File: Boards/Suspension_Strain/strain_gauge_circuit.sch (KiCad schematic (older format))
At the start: 9 parts, among them U101 MCP6001T-I-LT

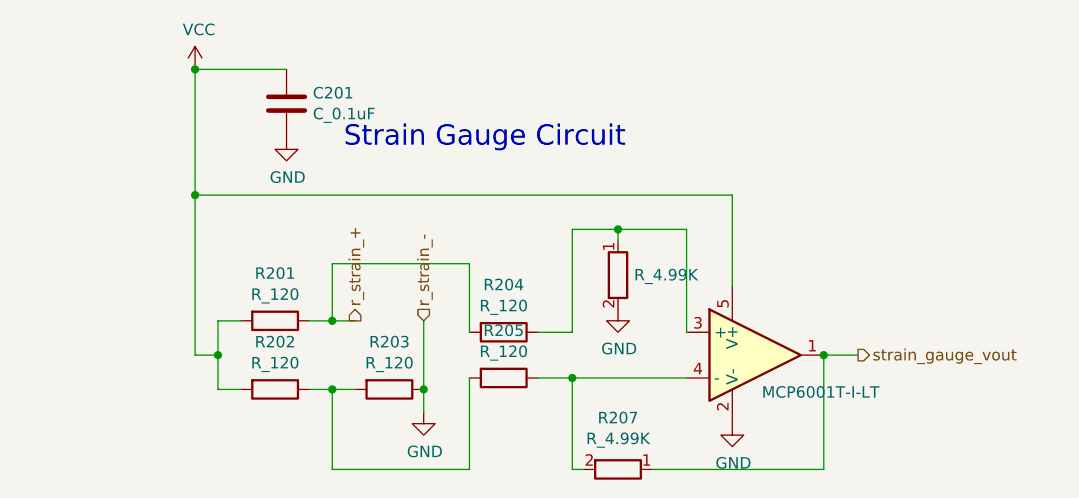
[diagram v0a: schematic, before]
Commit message: Add in-progress changes for reducing noise and component use
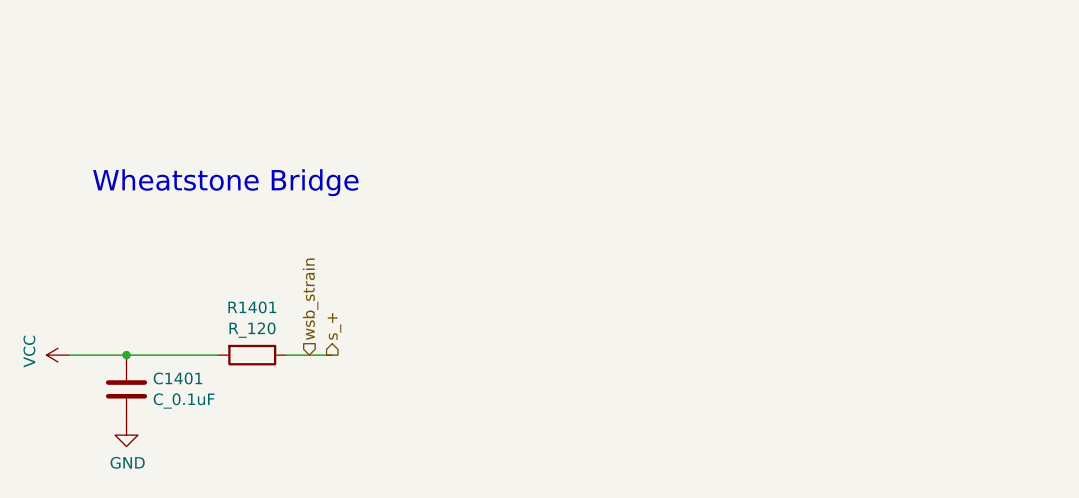
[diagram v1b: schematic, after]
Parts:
- removed R102, R103, R104, R105: R_120, footprints:R_0805_OEM, symbol Formula:R_120
- removed R106, R407: R_4.99K, footprints:R_0805_OEM, symbol Formula:R_4.99K
- removed U101: MCP6001T-I-LT, Package_TO_SOT_SMD:SOT-353_SC-70-5, symbol Formula:MCP6001T-I-LT
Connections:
- net r_strain_+ renamed s_+
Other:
- note added: "Wheatstone Bridge"
- note removed: "Strain Gauge Circuit"
- moved on the sheet: C1401, R1401
